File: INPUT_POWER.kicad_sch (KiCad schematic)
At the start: 5 parts, among them Q1 2N7002, U4 AP2112K-3.3

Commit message: Completed first iteration and reviews
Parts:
- removed Q1: 2N7002, Package_TO_SOT_SMD:SOT-23, symbol Transistor_FET:2N7002
- removed R5: 10k, symbol Device:R
- added 3V3, BattMeas1, Vbatt1: TestPoint, TestPoint:TestPoint_Pad_D1.0mm, symbol Connector:TestPoint
- added C20, C21: 1uF, Capacitor_SMD:C_0805_2012Metric_Pad1.18x1.45mm_HandSolder, symbol Device:C
- added C22: 10nF, Capacitor_SMD:C_0805_2012Metric_Pad1.18x1.45mm_HandSolder, symbol Device:C
- added D1: MBR0530, Diode_SMD:D_SOD-123, symbol Diode:MBR0530
- R3, R4: value 200k -> 500k; footprint (none) -> Resistor_SMD:R_0805_2012Metric_Pad1.20x1.40mm_HandSolder; Supplier (none) -> Digikey; Supplier Part Number (none) -> 738-RNCF0805BTE500KCT-ND
- U4: Supplier (none) -> Digikey; Supplier Part Number (none) -> AP2112K-3.3TRG1DICT-ND
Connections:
- net 3V3: now also 3V3.1, C21.2
- net Battery_Voltage: now also BattMeas1.1, C22.1
- net GND: now also R4.2, C20.1, C21.1, C22.2
- net Vbatt: now also D1.2 (A), Vbatt1.1; no longer U4.1 (VIN), U4.3 (EN)
- new net: C20.2, D1.1 (K), U4.1 (VIN), U4.3 (EN)
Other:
- sheet Qi wireless charging renamed Qi wireless power
- sheet Qi wireless power: file qi_wireless_charging.kicad_sch -> qi_wireless_power.kicad_sch
- company: (none) -> Horatio Pistachio
- title: (none) -> WashingLineMonitor-P0001

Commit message: commit of local files before designing next version
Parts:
- D1: JLC_Part_Number (none) -> C77336
- U4: JLC_Part_Number (none) -> C51118
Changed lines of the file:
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@@
+			)
+		)
+		(property "JLC_Part_Number" ""
+			(at 59.69 153.67 0)
+			(effects
+				(font
+					(size 1.27 1.27)
+				)
+				(hide yes)
 			)
 		)
@@
 			)
 		)
+		(property "JLC_Part_Number" ""
+			(at 129.54 152.4 0)
+			(effects
+				(font
+					(size 1.27 1.27)
+				)
+				(hide yes)
+			)
+		)
 		(pin "2"
 		)
@@
 			)
 		)
+		(property "JLC_Part_Number" ""
+			(at 46.99 142.24 90)
+			(effects
+				(font
+					(size 1.27 1.27)
+				)
+				(hide yes)
+			)
+		)
 		(pin "1"
 		)
@@
 			)
 		)
+		(property "JLC_Part_Number" ""
+			(at 46.99 148.59 0)
+			(effects
+				(font
+					(size 1.27 1.27)
+				)
+				(hide yes)
+			)
+		)
 		(pin "1"
 		)
@@
 			)
 		)
+		(property "JLC_Part_Number" ""
+			(at 163.83 152.4 0)
+			(effects
+				(font
+					(size 1.27 1.27)
+				)
+				(hide yes)
+			)
+		)
 		(pin "2"
 		)
@@
 			)
 		)
+		(property "JLC_Part_Number" ""
+			(at 167.64 146.05 0)
+			(effects
+				(font
+					(size 1.27 1.27)
+				)
+				(hide yes)
+			)
+		)
 		(pin "1"
 		)
@@
 			)
 		)
+		(property "JLC_Part_Number" ""
+			(at 46.99 160.02 0)
+			(effects
+				(font
+					(size 1.27 1.27)
+				)
+				(hide yes)
+			)
+		)
 		(pin "1"
 		)
@@
 			)
 		)
+		(property "JLC_Part_Number" ""
+			(at 59.69 157.48 0)
+			(effects
+				(font
+					(size 1.27 1.27)
+				)
+				(hide yes)
+			)
+		)
 		(pin "2"
 		)
@@
 			)
 		)
+		(property "JLC_Part_Number" "C77336"
+			(at 123.19 148.59 0)
+			(effects
+				(font
+					(size 1.27 1.27)
+				)
+				(hide yes)
+			)
+		)
 		(pin "2"
 		)
@@
 			(at 151.13 151.13 0)
 			(effects
+				(font
+					(size 1.27 1.27)
+				)
+				(hide yes)
+			)
+		)
+		(property "JLC_Part_Number" "C51118 "
+			(at 151.13 151.13 0)
+			(effects

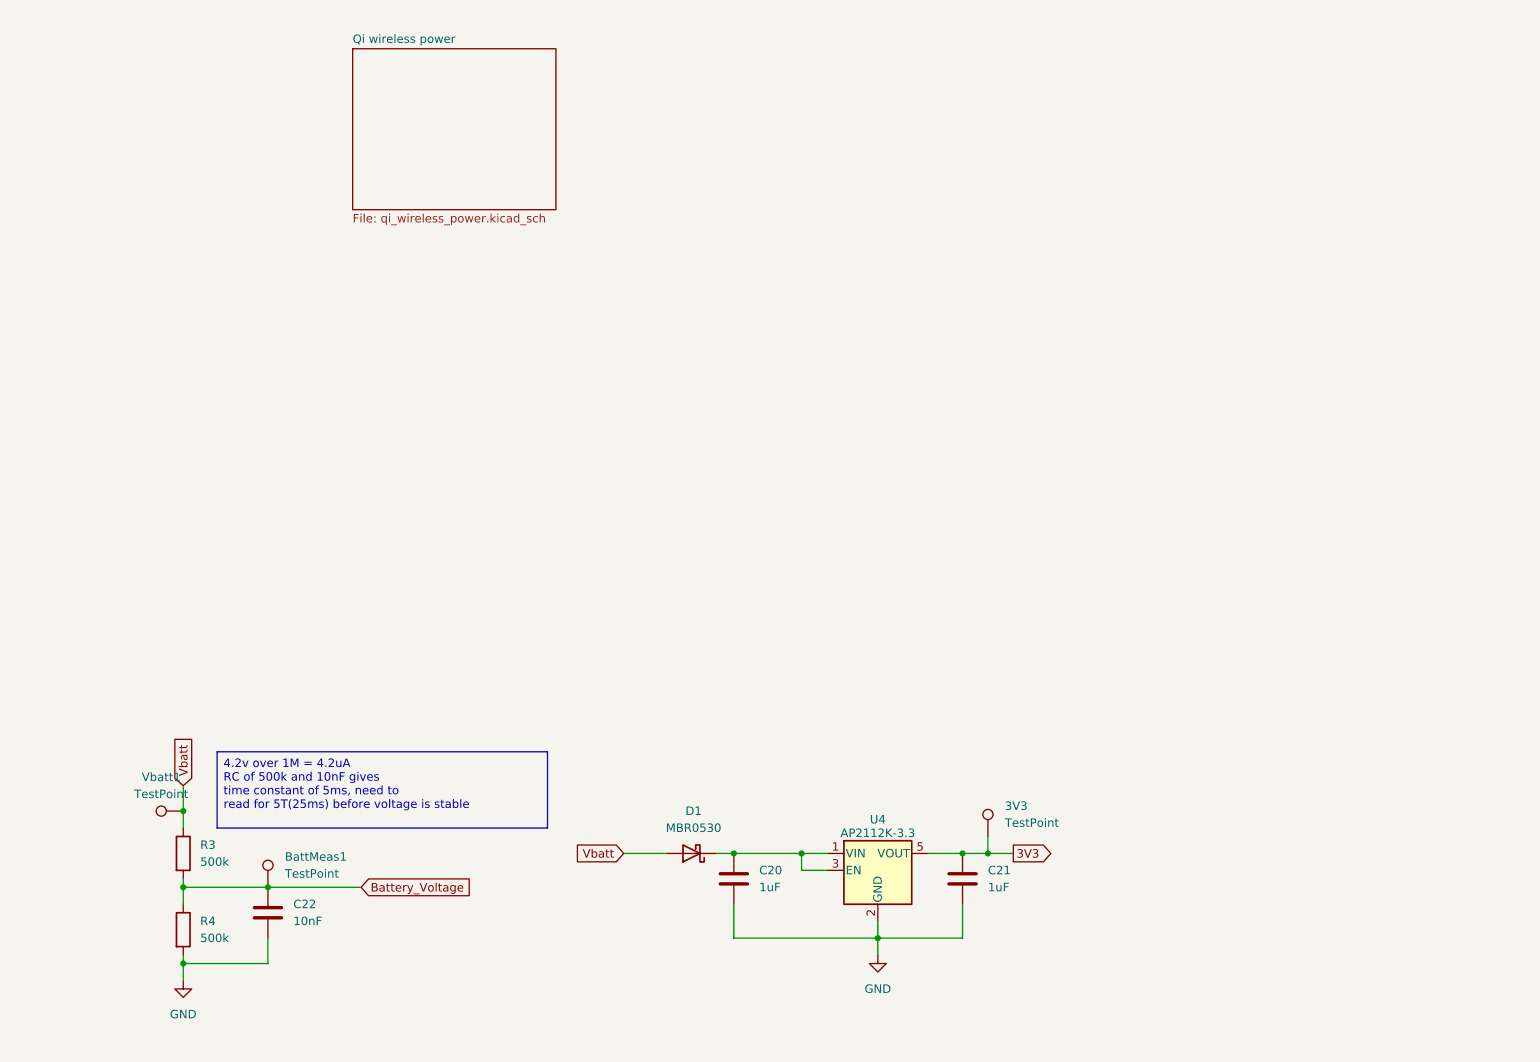
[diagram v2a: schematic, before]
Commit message: updated schematic from review
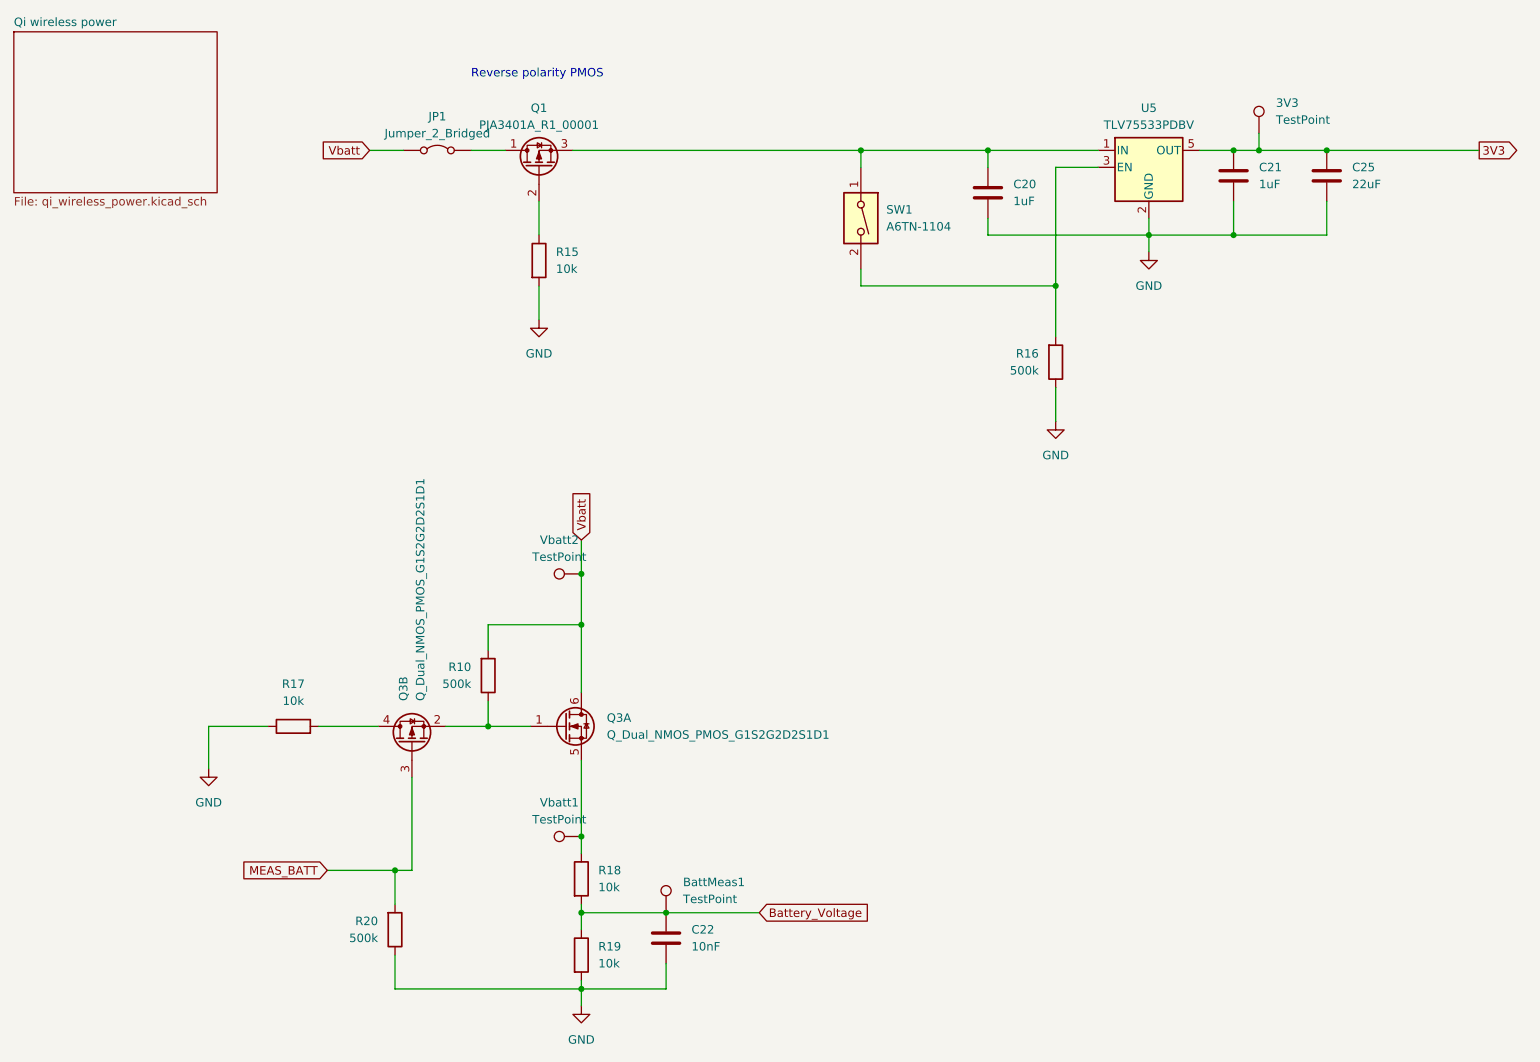
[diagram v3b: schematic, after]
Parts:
- removed D1: MBR0530, Diode_SMD:D_SOD-123, symbol Diode:MBR0530
- removed R3, R4: 500k, Resistor_SMD:R_0805_2012Metric_Pad1.20x1.40mm_HandSolder, symbol Device:R
- removed U4: AP2112K-3.3, Package_TO_SOT_SMD:SOT-23-5, symbol Regulator_Linear:AP2112K-3.3
- added C25: 22uF, Capacitor_SMD:C_0805_2012Metric_Pad1.18x1.45mm_HandSolder, symbol Device:C
- added JP1: Jumper_2_Bridged, Jumper:SolderJumper-2_P1.3mm_Bridged_RoundedPad1.0x1.5mm, symbol Jumper:Jumper_2_Bridged
- added Q1: PJA3401A_R1_00001, Package_TO_SOT_SMD:SOT-23, symbol Transistor_FET:Q_PMOS_DGS
- added Q3: Q_Dual_NMOS_PMOS_G1S2G2D2S1D1, Package_SO:TSOP-6_1.65x3.05mm_P0.95mm, symbol Transistor_FET:Q_Dual_NMOS_PMOS_G1S2G2D2S1D1
- added R10, R16, R20: 500k, Resistor_SMD:R_0805_2012Metric_Pad1.20x1.40mm_HandSolder, symbol Device:R
- added R15, R17, R18, R19: 10k, Resistor_SMD:R_0805_2012Metric_Pad1.20x1.40mm_HandSolder, symbol Device:R
- added SW1: A6TN-1104, Button_Switch_THT:SW_DIP_SPSTx01_Slide_6.7x4.1mm_W7.62mm_P2.54mm_LowProfile, symbol Switch:SW_DIP_x01
- added U5: TLV75533PDBV, Package_TO_SOT_SMD:SOT-23-5, symbol Regulator_Linear:TLV75533PDBV
- added Vbatt2: TestPoint, TestPoint:TestPoint_Pad_D1.0mm, symbol Connector:TestPoint
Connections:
- net 3V3: now also C25.1, U5.5 (OUT)
- net Battery_Voltage: now also R18.2, R19.1
- net GND: now also C25.2, R15.2, R16.1, R17.1, R19.2, R20.1, U5.2 (GND)
- net Vbatt: now also JP1.1 (A), Q3.6 (D), R10.2, Vbatt2.1; no longer Vbatt1.1
- net at C20.2: now also Q1.3 (S), SW1.1, U5.1 (IN)
- new net: JP1.2 (B), Q1.1 (D)
- new net: Q1.2 (G), R15.1
- new net: Q3.1 (G), Q3.2 (S), R10.1
- new net: Q3.5 (S), R18.1, Vbatt1.1
- new net: Q3.4 (D), R17.2
- new net: R16.2, SW1.2, U5.3 (EN)
- new net MEAS_BATT: Q3.3 (G), R20.2
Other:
- note added: "Reverse polarity PMOS"
- moved on the sheet: 3V3, BattMeas1, C20, C21, C22, Vbatt1

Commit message: laid out pcb
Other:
- moved on the sheet: JP1
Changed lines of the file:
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@@
 	(wire
 		(pts
-			(xy 74.93 43.18) (xy 80.01 43.18)
+			(xy 68.58 43.18) (xy 76.2 43.18)
 		)
 		(stroke
@@
 	(wire
 		(pts
-			(xy 90.17 43.18) (xy 95.25 43.18)
+			(xy 86.36 43.18) (xy 95.25 43.18)
 		)
 		(stroke
@@
 	(global_label "Vbatt"
 		(shape input)
-		(at 74.93 43.18 180)
+		(at 68.58 43.18 180)
 		(fields_autoplaced yes)
 		(effects
@@
 		)
 		(property "Intersheetrefs" "${INTERSHEET_REFS}"
-			(at 67.1068 43.18 0)
+			(at 60.7568 43.18 0)
 			(hide yes)
 			(show_name no)
@@
 	(symbol
 		(lib_id "Jumper:Jumper_2_Bridged")
-		(at 85.09 43.18 0)
+		(at 81.28 43.18 0)
 		(unit 1)
 		(body_style 1)
@@
 		(fields_autoplaced yes)
 		(property "Reference" "JP1"
-			(at 85.09 38.1 0)
+			(at 81.28 38.1 0)
 			(show_name no)
 			(do_not_autoplace no)
@@
 		)
 		(property "Value" "Jumper_2_Bridged"
-			(at 85.09 40.64 0)
+			(at 81.28 40.64 0)
 			(show_name no)
 			(do_not_autoplace no)
@@
 		)
 		(property "Footprint" "Jumper:SolderJumper-2_P1.3mm_Bridged_RoundedPad1.0x1.5mm"
-			(at 85.09 43.18 0)
+			(at 81.28 43.18 0)
 			(hide yes)
 			(show_name no)
@@
 		)
 		(property "Datasheet" ""
-			(at 85.09 43.18 0)
+			(at 81.28 43.18 0)
 			(hide yes)
 			(show_name no)
@@
 		)
 		(property "Description" "Jumper, 2-pole, closed/bridged"
-			(at 85.09 43.18 0)
+			(at 81.28 43.18 0)
 			(hide yes)
 			(show_name no)
@@
 		)
 		(property "Availability" ""
-			(at 85.09 43.18 0)
+			(at 81.28 43.18 0)
 			(hide yes)
 			(show_name no)
@@
 		)
 		(property "Check_prices" ""
-			(at 85.09 43.18 0)
+			(at 81.28 43.18 0)
 			(hide yes)
 			(show_name no)
@@
 		)
 		(property "Description_1" ""
-			(at 85.09 43.18 0)
+			(at 81.28 43.18 0)
 			(hide yes)
 			(show_name no)
@@
 		)
 		(property "MANUFACTURER" ""
-			(at 85.09 43.18 0)
+			(at 81.28 43.18 0)
 			(hide yes)
 			(show_name no)
@@
 		)
 		(property "MAXIMUM_PACKAGE_HEIGHT" ""
-			(at 85.09 43.18 0)
+			(at 81.28 43.18 0)
 			(hide yes)
 			(show_name no)
@@
 		)
 		(property "MF" ""
-			(at 85.09 43.18 0)
+			(at 81.28 43.18 0)
 			(hide yes)
 			(show_name no)
@@
 		)
 		(property "MP" ""
-			(at 85.09 43.18 0)
+			(at 81.28 43.18 0)
 			(hide yes)
 			(show_name no)
@@
 		)
 		(property "PARTREV" ""
-			(at 85.09 43.18 0)
+			(at 81.28 43.18 0)
 			(hide yes)
 			(show_name no)
@@
 		)
 		(property "Package" ""
-			(at 85.09 43.18 0)
+			(at 81.28 43.18 0)
 			(hide yes)
 			(show_name no)
@@
 		)
 		(property "Price" ""
-			(at 85.09 43.18 0)
+			(at 81.28 43.18 0)
 			(hide yes)
 			(show_name no)
@@
 		)
 		(property "Purchase-URL" ""
-			(at 85.09 43.18 0)
+			(at 81.28 43.18 0)
 			(hide yes)
 			(show_name no)
@@
 		)
 		(property "STANDARD" ""
-			(at 85.09 43.18 0)
+			(at 81.28 43.18 0)
 			(hide yes)
 			(show_name no)
@@
 		)
 		(property "SnapEDA_Link" ""
-			(at 85.09 43.18 0)
+			(at 81.28 43.18 0)
 			(hide yes)
 			(show_name no)

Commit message: Near complete AC
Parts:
- Q1: symbol Transistor_FET:Q_PMOS_DGS -> Transistor_FET:Q_PMOS_GSD
- renumbered Vbatt2 to TP5, Vbatt1 to TP6, BattMeas1 to TP7, 3V3 to TP8
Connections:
- net at Q1.1 (G): now also R15.1; no longer JP1.2 (B)
- net at Q1.2 (S): now also C20.2, SW1.1, U5.1 (IN); no longer R15.1
- new net: JP1.2 (B), Q1.3 (D)
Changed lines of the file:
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@@
 	)
 	(symbol
-		(lib_id "Transistor_FET:Q_PMOS_DGS")
+		(lib_id "Transistor_FET:Q_PMOS_GSD")
 		(at 100.33 45.72 90)
 		(unit 1)
@@
 			)
 		)
-		(property "Description" "P-MOSFET transistor, drain/gate/source"
+		(property "Description" "P-MOSFET transistor, gate/source/drain"
 			(at 100.33 45.72 0)
 			(hide yes)
@@
 		(dnp no)
 		(fields_autoplaced yes)
-		(property "Reference" "BattMeas1"
+		(property "Reference" "TP7"
 			(at 121.92 152.9079 0)
 			(show_name no)
@@
 			(project "WashingLineMonitor-P0001"
 				(path "/09468f75-1295-4aed-9d66-1cbb46f6d9f7/fe242c69-4638-4ad9-952b-9c215da932fb"
-					(reference "BattMeas1")
+					(reference "TP7")
 					(unit 1)
 				)
@@
 		(dnp no)
 		(fields_autoplaced yes)
-		(property "Reference" "Vbatt2"
+		(property "Reference" "TP5"
 			(at 103.378 101.6 90)
 			(show_name no)
@@
 			(project "WashingLineMonitor-P0001"
 				(path "/09468f75-1295-4aed-9d66-1cbb46f6d9f7/fe242c69-4638-4ad9-952b-9c215da932fb"
-					(reference "Vbatt2")
+					(reference "TP5")
 					(unit 1)
 				)
@@
 		(dnp no)
 		(fields_autoplaced yes)
-		(property "Reference" "Vbatt1"
+		(property "Reference" "TP6"
 			(at 103.378 140.97 90)
 			(show_name no)
@@
 			(project "WashingLineMonitor-P0001"
 				(path "/09468f75-1295-4aed-9d66-1cbb46f6d9f7/fe242c69-4638-4ad9-952b-9c215da932fb"
-					(reference "Vbatt1")
+					(reference "TP6")
 					(unit 1)
 				)
@@
 		(dnp no)
 		(fields_autoplaced yes)
-		(property "Reference" "3V3"
+		(property "Reference" "TP8"
 			(at 210.82 36.0679 0)
 			(show_name no)
@@
 			(project "WashingLineMonitor-P0001"
 				(path "/09468f75-1295-4aed-9d66-1cbb46f6d9f7/fe242c69-4638-4ad9-952b-9c215da932fb"
-					(reference "3V3")
+					(reference "TP8")
 					(unit 1)
 				)

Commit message: Minor pre release changes
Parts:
- JP1, TP5, TP6, TP7, TP8: now left out of the parts list
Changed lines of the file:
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@@
 	(title_block
 		(title "WashingLineMonitor-P0001")
-		(date "2025-09-14")
-		(rev "AB")
+		(date "2026-06-06")
+		(rev "AC")
 		(company "Horatio Pistachio")
 	)
@@
 		(body_style 1)
 		(exclude_from_sim no)
-		(in_bom yes)
+		(in_bom no)
 		(on_board yes)
 		(in_pos_files yes)
@@
 		(body_style 1)
 		(exclude_from_sim no)
-		(in_bom yes)
+		(in_bom no)
 		(on_board yes)
 		(in_pos_files yes)
@@
 		(body_style 1)
 		(exclude_from_sim no)
-		(in_bom yes)
+		(in_bom no)
 		(on_board yes)
 		(in_pos_files yes)
@@
 		(body_style 1)
 		(exclude_from_sim no)
-		(in_bom yes)
+		(in_bom no)
 		(on_board yes)
 		(in_pos_files yes)
@@
 		(body_style 1)
 		(exclude_from_sim no)
-		(in_bom yes)
+		(in_bom no)
 		(on_board yes)
 		(in_pos_files yes)
